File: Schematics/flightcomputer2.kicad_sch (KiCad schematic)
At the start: 0 parts

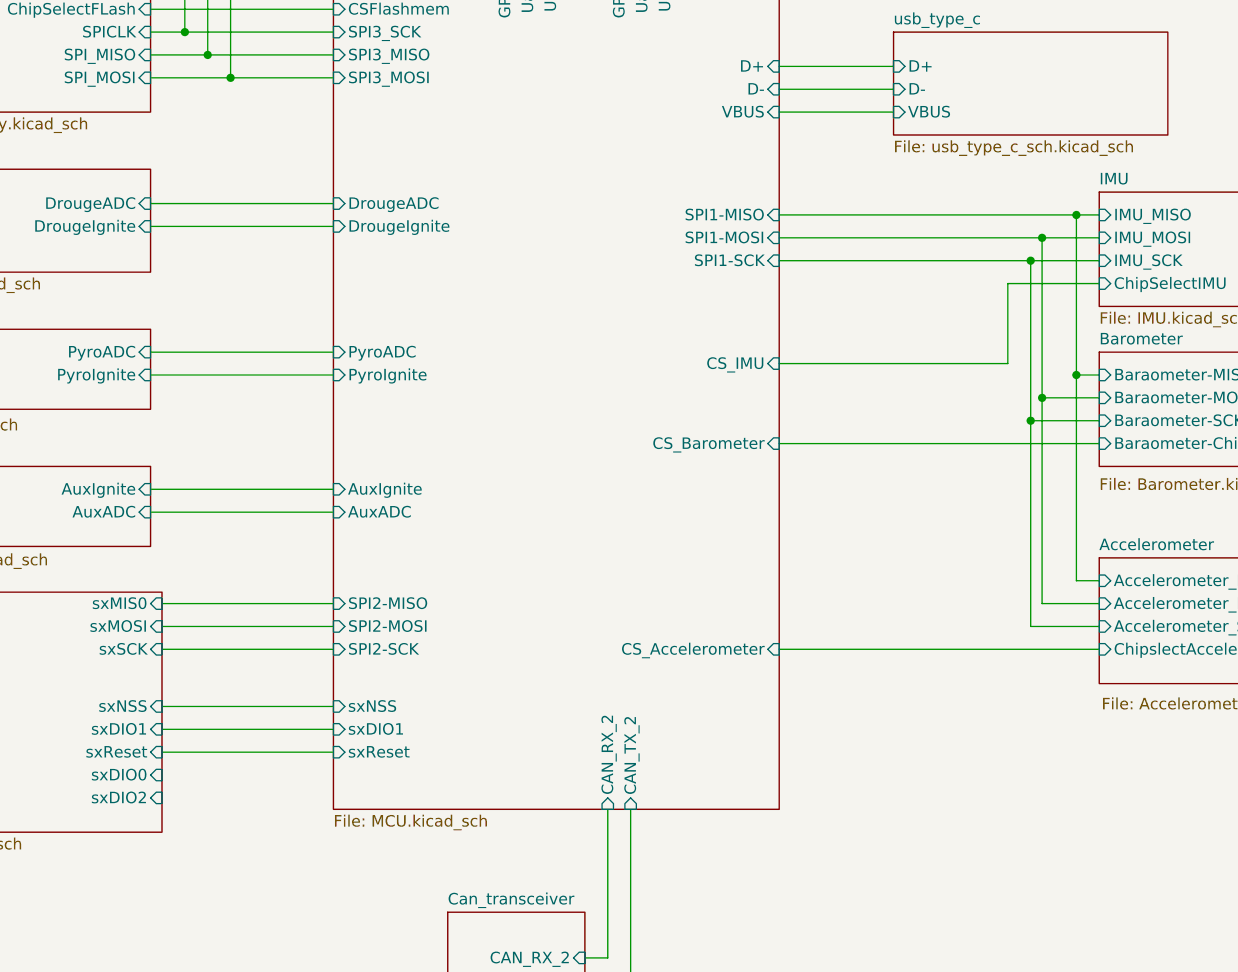
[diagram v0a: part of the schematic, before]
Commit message: reviewed schematic and pcb and replaced part numbers, added and named datasheets into document folder
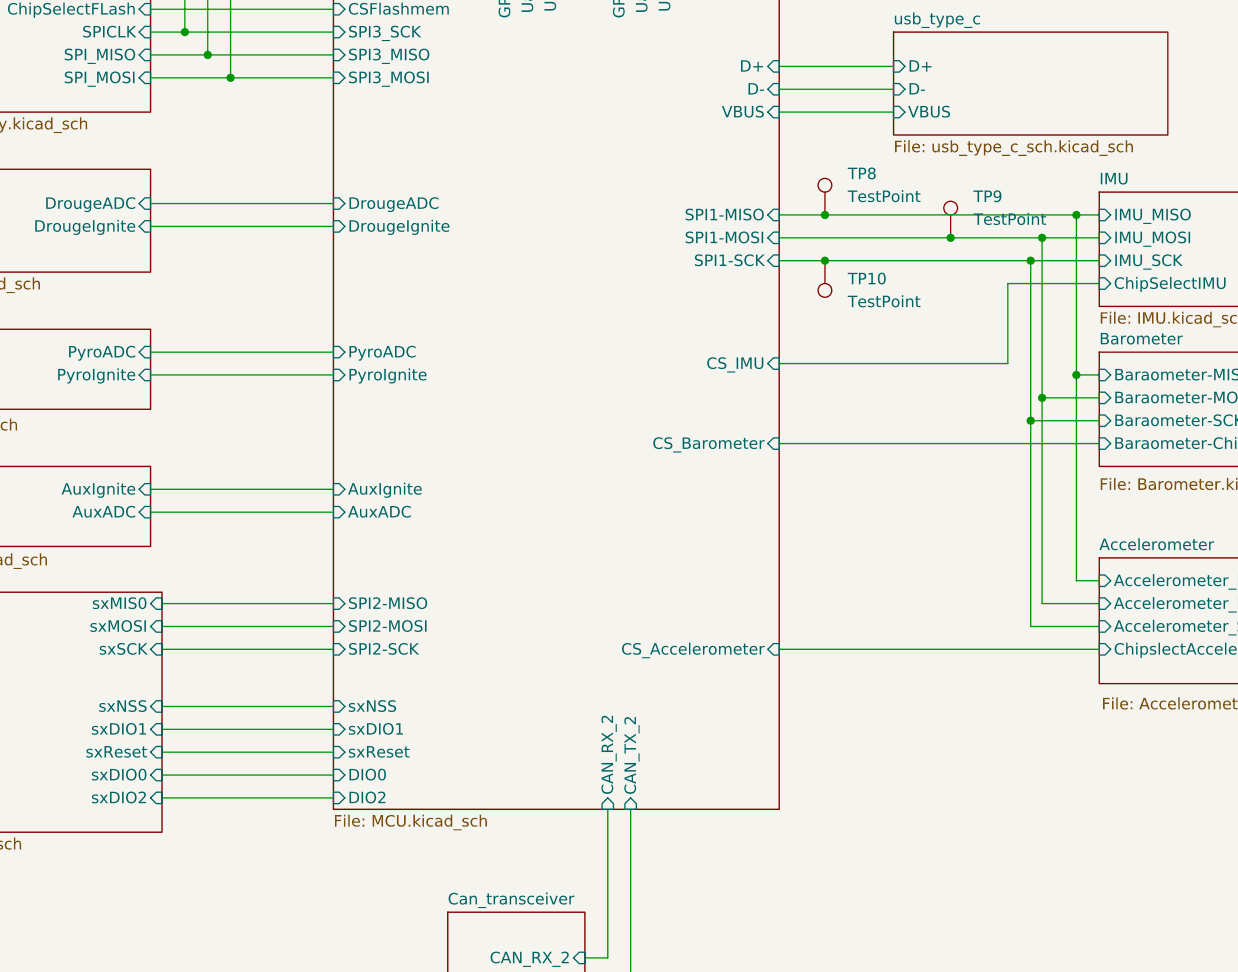
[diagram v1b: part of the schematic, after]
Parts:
- added TP10, TP8, TP9: TestPoint, TestPoint:TestPoint_Pad_1.5x1.5mm, symbol Connector:TestPoint
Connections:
- net Accelerometer/Accelerometer_MIS0: now also TP8.1
- net Accelerometer/Accelerometer_MOSI: now also TP9.1
- net Accelerometer/Accelerometer_SPICLK: now also TP10.1
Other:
- sheet MCU ports: added DIO0, DIO2; removed none

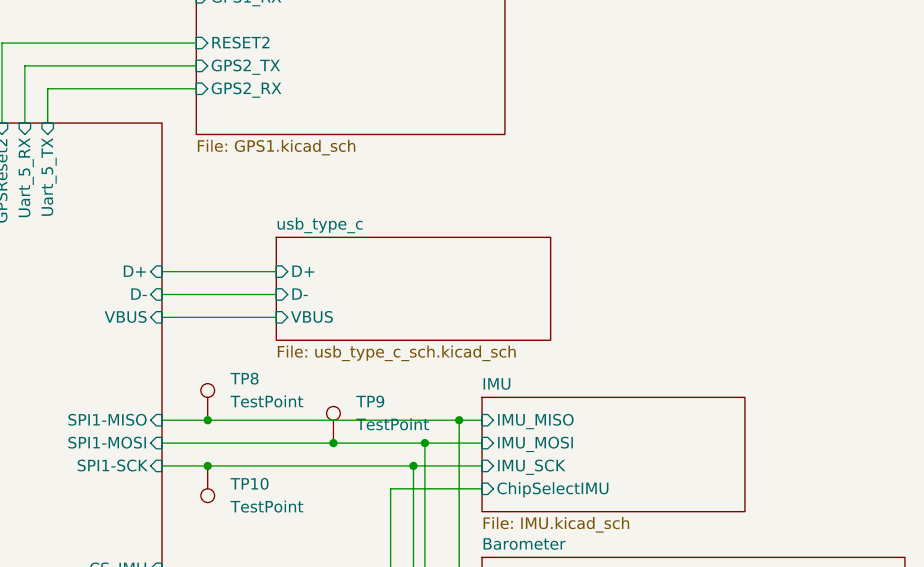
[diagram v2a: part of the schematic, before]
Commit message: Fixing ldo pinout, updated lora drivers need to still write final function such as lora sleep ect
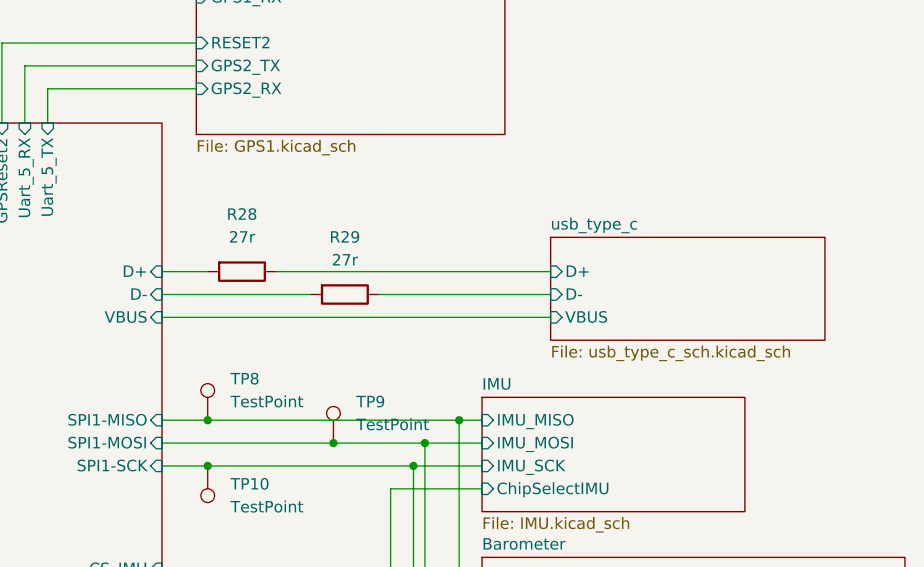
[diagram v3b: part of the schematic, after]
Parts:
- added R28, R29: 27r, Resistor_SMD:R_0805_2012Metric_Pad1.20x1.40mm_HandSolder, symbol Device:R
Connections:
- net MCU/D+: now also R28.2
- net MCU/D-: now also R29.2
- new net usb_type_c/D+: R28.1
- new net usb_type_c/D-: R29.1
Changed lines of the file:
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@@
+	(wire
+		(pts
+			(xy 173.99 66.04) (xy 204.47 66.04)
+		)
+		(stroke
+			(width 0)
+			(type default)
+		)
+	)
 	(wire
 		(pts
@@
 	(wire
 		(pts
-			(xy 161.29 71.12) (xy 173.99 71.12)
+			(xy 161.29 71.12) (xy 204.47 71.12)
 		)
 		(stroke
@@
 	(wire
 		(pts
-			(xy 161.29 68.58) (xy 173.99 68.58)
+			(xy 161.29 68.58) (xy 177.8 68.58)
 		)
 		(stroke
@@
 	(wire
 		(pts
-			(xy 161.29 66.04) (xy 173.99 66.04)
+			(xy 161.29 66.04) (xy 166.37 66.04)
 		)
 		(stroke
@@
 		(pts
 			(xy 90.17 44.45) (xy 97.79 44.45)
+		)
+		(stroke
+			(width 0)
+			(type default)
+		)
+	)
+	(wire
+		(pts
+			(xy 185.42 68.58) (xy 204.47 68.58)
 		)
 		(stroke
@@
 	)
 	(symbol
+		(lib_id "Device:R")
+		(at 181.61 68.58 270)
+		(unit 1)
+		(body_style 1)
+		(exclude_from_sim no)
+		(in_bom yes)
+		(on_board yes)
+		(in_pos_files yes)
+		(dnp no)
+		(fields_autoplaced yes)
+		(property "Reference" "R29"
+			(at 181.61 62.23 90)
+			(show_name no)
+			(do_not_autoplace no)
+			(effects
+				(font
+					(size 1.27 1.27)
+				)
+			)
+		)
+		(property "Value" "27r"
+			(at 181.61 64.77 90)
+			(show_name no)
+			(do_not_autoplace no)
+			(effects
+				(font
+					(size 1.27 1.27)
+				)
+			)
+		)
+		(property "Footprint" "Resistor_SMD:R_0805_2012Metric_Pad1.20x1.40mm_HandSolder"
+			(at 181.61 66.802 90)
+			(hide yes)
+			(show_name no)
+			(do_not_autoplace no)
+			(effects
+				(font
+					(size 1.27 1.27)
+				)
+			)
+		)
+		(property "Datasheet" ""
+			(at 181.61 68.58 0)
+			(hide yes)
+			(show_name no)
+			(do_not_autoplace no)
+			(effects
+				(font
+					(size 1.27 1.27)
+				)
+			)
+		)
+		(property "Description" "Resistor"
+			(at 181.61 68.58 0)
+			(hide yes)
+			(show_name no)
+			(do_not_autoplace no)
+			(effects
+				(font
+					(size 1.27 1.27)
+				)
+			)
+		)
+		(pin "1"
+		)
+		(pin "2"
+		)
+		(instances
+			(project "flightcomputer2"
+				(path "/6cb3dda3-5fe8-4715-b831-354360aa3199"
+					(reference "R29")
+					(unit 1)
+				)
+			)
+		)
+	)
+	(symbol
+		(lib_id "Device:R")
+		(at 170.18 66.04 270)
+		(unit 1)
+		(body_style 1)
+		(exclude_from_sim no)
+		(in_bom yes)
+		(on_board yes)
+		(in_pos_files yes)
+		(dnp no)
+		(fields_autoplaced yes)
+		(property "Reference" "R28"
+			(at 170.18 59.69 90)
+			(show_name no)
+			(do_not_autoplace no)
+			(effects
+				(font
+					(size 1.27 1.27)
+				)
+			)
+		)
+		(property "Value" "27r"
+			(at 170.18 62.23 90)
+			(show_name no)
+			(do_not_autoplace no)
+			(effects
+				(font
+					(size 1.27 1.27)
+				)
+			)
+		)
+		(property "Footprint" "Resistor_SMD:R_0805_2012Metric_Pad1.20x1.40mm_HandSolder"
+			(at 170.18 64.262 90)
+			(hide yes)
+			(show_name no)
+			(do_not_autoplace no)
+			(effects
+				(font
+					(size 1.27 1.27)
+				)
+			)
+		)
+		(property "Datasheet" ""
+			(at 170.18 66.04 0)
+			(hide yes)
+			(show_name no)
+			(do_not_autoplace no)
+			(effects
+				(font
+					(size 1.27 1.27)
+				)
+			)
+		)
+		(property "Description" "Resistor"
+			(at 170.18 66.04 0)
+			(hide yes)
+			(show_name no)
+			(do_not_autoplace no)
+			(effects
+				(font
+					(size 1.27 1.27)
+				)
+			)
+		)
+		(pin "1"
+		)
+		(pin "2"
+		)
+		(instances
+			(project "flightcomputer2"
+				(path "/6cb3dda3-5fe8-4715-b831-354360aa3199"
+					(reference "R28")
+					(unit 1)
+				)
+			)
+		)
+	)
+	(symbol
 		(lib_id "Connector:TestPoint")
 		(at 166.37 87.63 180)
@@
 	)
 	(sheet
-		(at 173.99 62.23)
+		(at 204.47 62.23)
 		(size 30.48 11.43)
 		(exclude_from_sim no)
@@
 		)
 		(property "Sheetname" "usb_type_c"
-			(at 173.99 61.5184 0)
+			(at 204.47 61.5184 0)
 			(show_name no)
 			(do_not_autoplace no)
@@
 		)
 		(property "Sheetfile" "usb_type_c_sch.kicad_sch"
-			(at 173.99 74.2446 0)
+			(at 204.47 74.2446 0)
 			(show_name no)
 			(do_not_autoplace no)
@@
 		)
 		(pin "D+" input
-			(at 173.99 66.04 180)
+			(at 204.47 66.04 180)
 			(effects
 				(font
@@
 		)
 		(pin "D-" input
-			(at 173.99 68.58 180)
+			(at 204.47 68.58 180)
 			(effects
 				(font
@@
 		)
 		(pin "VBUS" input
-			(at 173.99 71.12 180)
-			(effects
-				(font
+			(at 204.47 71.12 180)
+			(effects
+				(font
